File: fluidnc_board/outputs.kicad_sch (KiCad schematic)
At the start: 20 parts

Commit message: remove unnecessary i2s chip
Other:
- title: (none) -> Configurable Outputs
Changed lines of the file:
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@@
 (kicad_sch (version 20211123) (generator eeschema)
   (paper "A4")
+  (title_block
+    (title "Configurable Outputs")
+  )
   (junction (at 137.16 132.715) (diameter 0) (color 0 0 0 0)
   )

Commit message: footprint associations and part no.
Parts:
- D58, D59, D60, D61: renamed from D?; Digikey Part No. (none) -> 1514-BZX84C5V6TRPBFREECT-ND
- J31, J32, J33, J34: renamed from J?; footprint (none) -> Connector_Phoenix_MC:PhoenixContact_MC_1,5_2-G-3.81_1x02_P3.81mm_Horizontal
- JP13, JP14, JP15, JP16: renamed from JP?; footprint (none) -> Jumper:SolderJumper-3_P1.3mm_Open_RoundedPad1.0x1.5mm_NumberLabels
- Q11, Q12, Q13, Q14: renamed from MOSFET?; footprint SO-8_INF -> Package_SO:SO-8_3.9x4.9mm_P1.27mm; Digikey Part No. (none) -> IRF7809AVPBFCT-ND
- R116, R117, R118, R119: renamed from R?; footprint (none) -> Resistor_SMD:R_0805_2012Metric_Pad1.20x1.40mm_HandSolder; Digikey Part No. (none) -> 311-10KARCT-ND

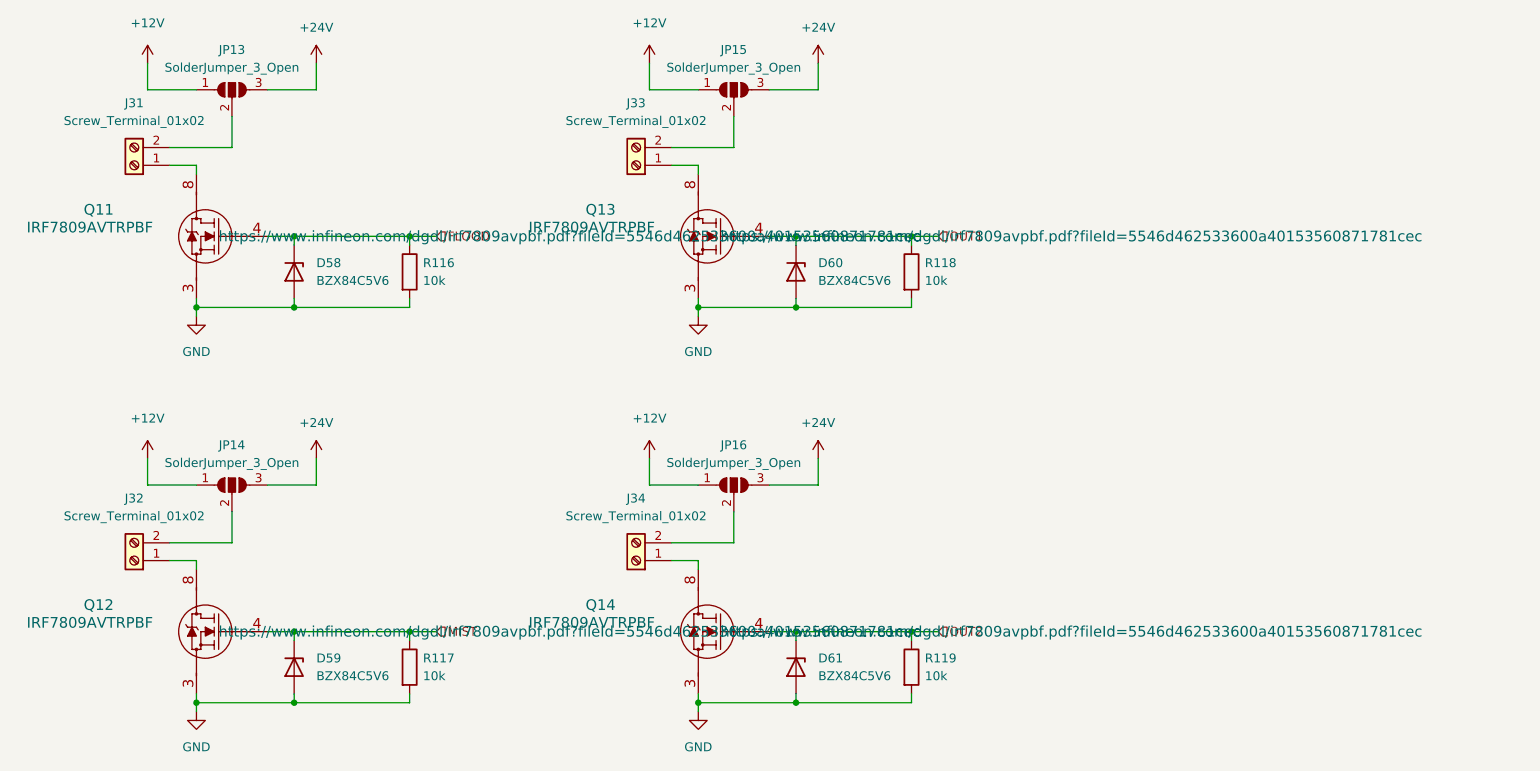
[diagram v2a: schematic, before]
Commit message: fix some footprint associations
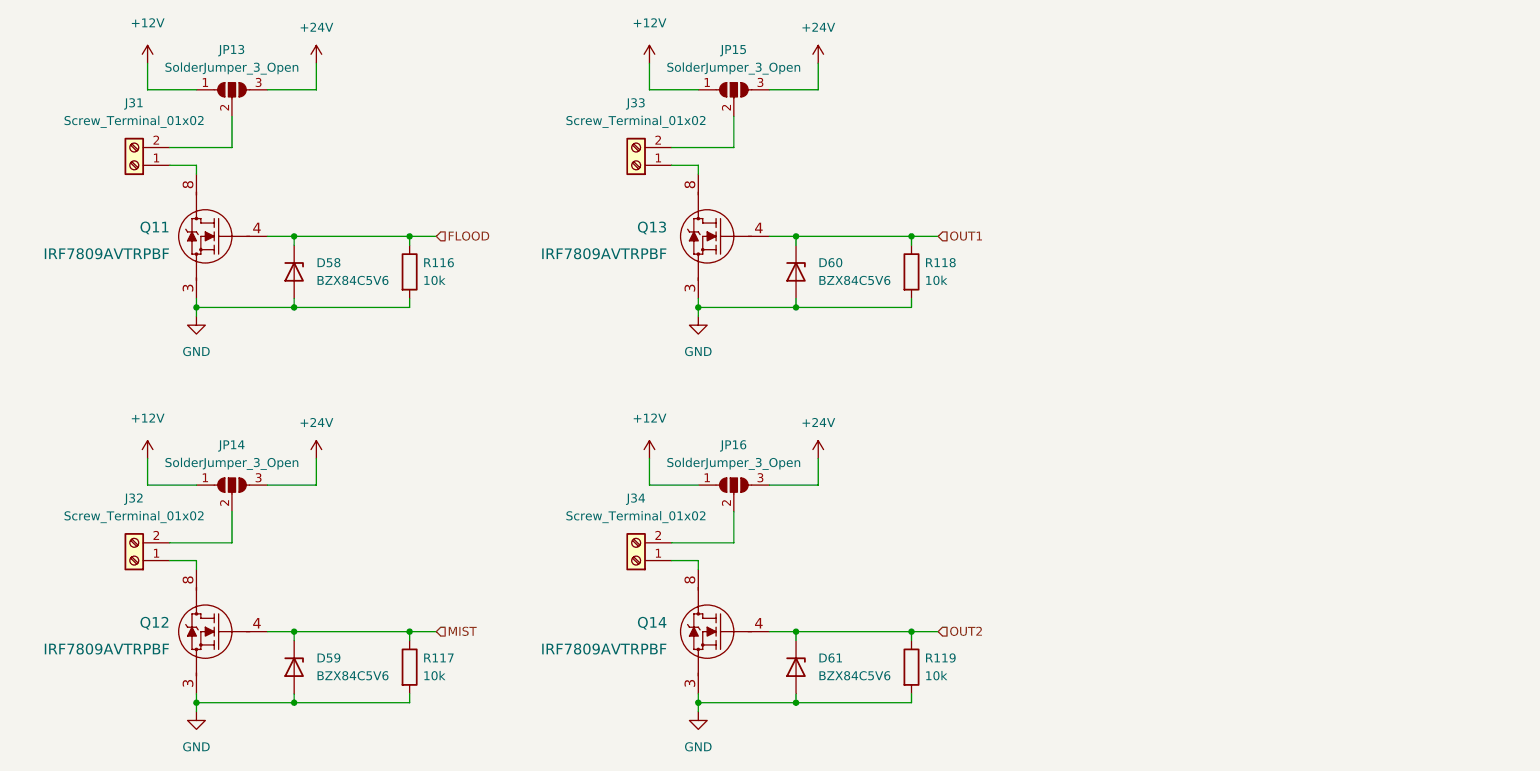
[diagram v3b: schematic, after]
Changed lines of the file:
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@@
   (symbol (lib_id "fluidnc_board:IRF7809AVTRPBF") (at 200.025 128.905 0) (mirror y) (unit 1)
     (in_bom yes) (on_board yes) (fields_autoplaced)
-    (property "Reference" "Q14" (id 0) (at 164.465 128.905 0)
-      (effects (font (size 1.524 1.524)))
-    )
-    (property "Value" "IRF7809AVTRPBF" (id 1) (at 163.195 131.445 0)
-      (effects (font (size 1.524 1.524)))
+    (property "Reference" "Q14" (id 0) (at 173.99 131.445 0)
+      (effects (font (size 1.524 1.524)) (justify left))
+    )
+    (property "Value" "IRF7809AVTRPBF" (id 1) (at 173.99 135.255 0)
+      (effects (font (size 1.524 1.524)) (justify left))
     )
     (property "Footprint" "Package_SO:SO-8_3.9x4.9mm_P1.27mm" (id 2) (at 163.195 133.985 0)
@@
     )
     (property "Datasheet" "https://www.infineon.com/dgdl/irf7809avpbf.pdf?fileId=5546d462533600a40153560871781cec" (id 3) (at 231.775 132.715 0)
-      (effects (font (size 1.524 1.524)))
+      (effects (font (size 1.524 1.524)) hide)
     )
     (property "Digikey Part No." "IRF7809AVPBFCT-ND" (id 4) (at 200.025 128.905 0)
@@
   (symbol (lib_id "fluidnc_board:IRF7809AVTRPBF") (at 128.27 72.39 0) (mirror y) (unit 1)
     (in_bom yes) (on_board yes) (fields_autoplaced)
-    (property "Reference" "Q11" (id 0) (at 92.71 72.39 0)
-      (effects (font (size 1.524 1.524)))
-    )
-    (property "Value" "IRF7809AVTRPBF" (id 1) (at 91.44 74.93 0)
-      (effects (font (size 1.524 1.524)))
+    (property "Reference" "Q11" (id 0) (at 102.87 74.93 0)
+      (effects (font (size 1.524 1.524)) (justify left))
+    )
+    (property "Value" "IRF7809AVTRPBF" (id 1) (at 102.87 78.74 0)
+      (effects (font (size 1.524 1.524)) (justify left))
     )
     (property "Footprint" "Package_SO:SO-8_3.9x4.9mm_P1.27mm" (id 2) (at 91.44 77.47 0)
@@
     )
     (property "Datasheet" "https://www.infineon.com/dgdl/irf7809avpbf.pdf?fileId=5546d462533600a40153560871781cec" (id 3) (at 160.02 76.2 0)
-      (effects (font (size 1.524 1.524)))
+      (effects (font (size 1.524 1.524)) hide)
     )
     (property "Digikey Part No." "IRF7809AVPBFCT-ND" (id 4) (at 128.27 72.39 0)
@@
   (symbol (lib_id "fluidnc_board:IRF7809AVTRPBF") (at 128.27 128.905 0) (mirror y) (unit 1)
     (in_bom yes) (on_board yes) (fields_autoplaced)
-    (property "Reference" "Q12" (id 0) (at 92.71 128.905 0)
-      (effects (font (size 1.524 1.524)))
-    )
-    (property "Value" "IRF7809AVTRPBF" (id 1) (at 91.44 131.445 0)
-      (effects (font (size 1.524 1.524)))
+    (property "Reference" "Q12" (id 0) (at 102.87 131.445 0)
+      (effects (font (size 1.524 1.524)) (justify left))
+    )
+    (property "Value" "IRF7809AVTRPBF" (id 1) (at 102.87 135.255 0)
+      (effects (font (size 1.524 1.524)) (justify left))
     )
     (property "Footprint" "Package_SO:SO-8_3.9x4.9mm_P1.27mm" (id 2) (at 91.44 133.985 0)
@@
     )
     (property "Datasheet" "https://www.infineon.com/dgdl/irf7809avpbf.pdf?fileId=5546d462533600a40153560871781cec" (id 3) (at 160.02 132.715 0)
-      (effects (font (size 1.524 1.524)))
+      (effects (font (size 1.524 1.524)) hide)
     )
     (property "Digikey Part No." "IRF7809AVPBFCT-ND" (id 4) (at 128.27 128.905 0)
@@
   (symbol (lib_id "fluidnc_board:IRF7809AVTRPBF") (at 200.025 72.39 0) (mirror y) (unit 1)
     (in_bom yes) (on_board yes) (fields_autoplaced)
-    (property "Reference" "Q13" (id 0) (at 164.465 72.39 0)
-      (effects (font (size 1.524 1.524)))
-    )
-    (property "Value" "IRF7809AVTRPBF" (id 1) (at 163.195 74.93 0)
-      (effects (font (size 1.524 1.524)))
+    (property "Reference" "Q13" (id 0) (at 173.99 74.93 0)
+      (effects (font (size 1.524 1.524)) (justify left))
+    )
+    (property "Value" "IRF7809AVTRPBF" (id 1) (at 173.99 78.74 0)
+      (effects (font (size 1.524 1.524)) (justify left))
     )
     (property "Footprint" "Package_SO:SO-8_3.9x4.9mm_P1.27mm" (id 2) (at 163.195 77.47 0)
@@
     )
     (property "Datasheet" "https://www.infineon.com/dgdl/irf7809avpbf.pdf?fileId=5546d462533600a40153560871781cec" (id 3) (at 231.775 76.2 0)
-      (effects (font (size 1.524 1.524)))
+      (effects (font (size 1.524 1.524)) hide)
     )
     (property "Digikey Part No." "IRF7809AVPBFCT-ND" (id 4) (at 200.025 72.39 0)

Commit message: fixed some footprint associations, placed footprints
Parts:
- D58, D59, D60, D61: Digikey Part No. 1514-BZX84C5V6TRPBFREECT-ND -> (none)
- Q11, Q12, Q13, Q14: Digikey Part No. IRF7809AVPBFCT-ND -> (none)
- R116, R117, R118, R119: Digikey Part No. 311-10KARCT-ND -> (none)
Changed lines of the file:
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@@
-      (effects (font (size 1.27 1.27)) hide)
-    )
-    (property "Digikey Part No." "1514-BZX84C5V6TRPBFREECT-ND" (id 4) (at 192.405 81.28 0)
       (effects (font (size 1.27 1.27)) hide)
     )
@@
       (effects (font (size 1.27 1.27)) hide)
     )
-    (property "Datasheet" "https://www.yageo.com/upload/media/product/productsearch/datasheet/rchip/PYu-RC_Group_51_RoHS_L_11.pdf" (id 3) (at 137.16 81.28 0)
-      (effects (font (size 1.27 1.27)) hide)
-    )
-    (property "Digikey Part No." "311-10KARCT-ND" (id 4) (at 137.16 81.28 0)
+    (property "Datasheet" "~" (id 3) (at 137.16 81.28 0)
       (effects (font (size 1.27 1.27)) hide)
     )
@@
       (effects (font (size 1.27 1.27)) hide)
     )
-    (property "Digikey Part No." "1514-BZX84C5V6TRPBFREECT-ND" (id 4) (at 192.405 137.795 0)
-      (effects (font (size 1.27 1.27)) hide)
-    )
     (pin "1")
     (pin "2")
@@
       (effects (font (size 1.27 1.27)) hide)
     )
-    (property "Digikey Part No." "1514-BZX84C5V6TRPBFREECT-ND" (id 4) (at 120.65 81.28 0)
-      (effects (font (size 1.27 1.27)) hide)
-    )
     (pin "1")
     (pin "2")
@@
       (effects (font (size 1.524 1.524)) hide)
     )
-    (property "Datasheet" "https://www.infineon.com/dgdl/irf7809avpbf.pdf?fileId=5546d462533600a40153560871781cec" (id 3) (at 231.775 132.715 0)
-      (effects (font (size 1.524 1.524)) hide)
-    )
-    (property "Digikey Part No." "IRF7809AVPBFCT-ND" (id 4) (at 200.025 128.905 0)
-      (effects (font (size 1.27 1.27)) hide)
+    (property "Datasheet" "" (id 3) (at 231.775 132.715 0)
+      (effects (font (size 1.524 1.524)) hide)
     )
     (pin "1")
@@
       (effects (font (size 1.27 1.27)) hide)
     )
-    (property "Datasheet" "https://www.yageo.com/upload/media/product/productsearch/datasheet/rchip/PYu-RC_Group_51_RoHS_L_11.pdf" (id 3) (at 208.915 137.795 0)
-      (effects (font (size 1.27 1.27)) hide)
-    )
-    (property "Digikey Part No." "311-10KARCT-ND" (id 4) (at 208.915 137.795 0)
+    (property "Datasheet" "~" (id 3) (at 208.915 137.795 0)
       (effects (font (size 1.27 1.27)) hide)
     )
@@
       (effects (font (size 1.524 1.524)) hide)
     )
-    (property "Datasheet" "https://www.infineon.com/dgdl/irf7809avpbf.pdf?fileId=5546d462533600a40153560871781cec" (id 3) (at 160.02 76.2 0)
-      (effects (font (size 1.524 1.524)) hide)
-    )
-    (property "Digikey Part No." "IRF7809AVPBFCT-ND" (id 4) (at 128.27 72.39 0)
-      (effects (font (size 1.27 1.27)) hide)
+    (property "Datasheet" "" (id 3) (at 160.02 76.2 0)
+      (effects (font (size 1.524 1.524)) hide)
     )
     (pin "1")
@@
       (effects (font (size 1.27 1.27)) hide)
     )
-    (property "Datasheet" "https://www.yageo.com/upload/media/product/productsearch/datasheet/rchip/PYu-RC_Group_51_RoHS_L_11.pdf" (id 3) (at 208.915 81.28 0)
-      (effects (font (size 1.27 1.27)) hide)
-    )
-    (property "Digikey Part No." "311-10KARCT-ND" (id 4) (at 208.915 81.28 0)
+    (property "Datasheet" "~" (id 3) (at 208.915 81.28 0)
       (effects (font (size 1.27 1.27)) hide)
     )
@@
       (effects (font (size 1.27 1.27)) hide)
     )
-    (property "Datasheet" "https://www.yageo.com/upload/media/product/productsearch/datasheet/rchip/PYu-RC_Group_51_RoHS_L_11.pdf" (id 3) (at 137.16 137.795 0)
-      (effects (font (size 1.27 1.27)) hide)
-    )
-    (property "Digikey Part No." "311-10KARCT-ND" (id 4) (at 137.16 137.795 0)
+    (property "Datasheet" "~" (id 3) (at 137.16 137.795 0)
       (effects (font (size 1.27 1.27)) hide)
     )
@@
       (effects (font (size 1.524 1.524)) hide)
     )
-    (property "Datasheet" "https://www.infineon.com/dgdl/irf7809avpbf.pdf?fileId=5546d462533600a40153560871781cec" (id 3) (at 160.02 132.715 0)
-      (effects (font (size 1.524 1.524)) hide)
-    )
-    (property "Digikey Part No." "IRF7809AVPBFCT-ND" (id 4) (at 128.27 128.905 0)
-      (effects (font (size 1.27 1.27)) hide)
+    (property "Datasheet" "" (id 3) (at 160.02 132.715 0)
+      (effects (font (size 1.524 1.524)) hide)
     )
     (pin "1")
@@
       (effects (font (size 1.524 1.524)) hide)
     )
-    (property "Datasheet" "https://www.infineon.com/dgdl/irf7809avpbf.pdf?fileId=5546d462533600a40153560871781cec" (id 3) (at 231.775 76.2 0)
-      (effects (font (size 1.524 1.524)) hide)
-    )
-    (property "Digikey Part No." "IRF7809AVPBFCT-ND" (id 4) (at 200.025 72.39 0)
-      (effects (font (size 1.27 1.27)) hide)
+    (property "Datasheet" "" (id 3) (at 231.775 76.2 0)
+      (effects (font (size 1.524 1.524)) hide)
     )
     (pin "1")
@@
       (effects (font (size 1.27 1.27)) hide)
     )
-    (property "Digikey Part No." "1514-BZX84C5V6TRPBFREECT-ND" (id 4) (at 120.65 137.795 0)
-      (effects (font (size 1.27 1.27)) hide)
-    )
